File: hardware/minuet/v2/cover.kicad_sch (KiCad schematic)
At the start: 12 parts, among them J401 B2B-XH-A, U401 DRV8876PWPR

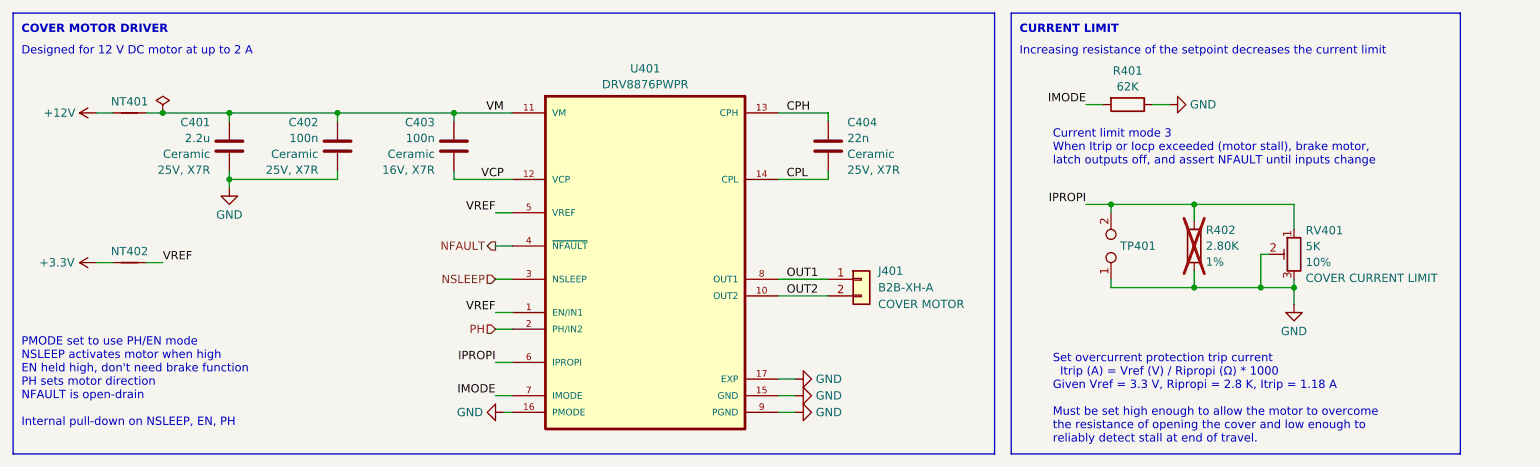
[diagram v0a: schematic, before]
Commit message: Finalize Minuet v2.1 for manufacture.
This revision uses a different motor controller and buck converter
and remedies errata from v2.0.
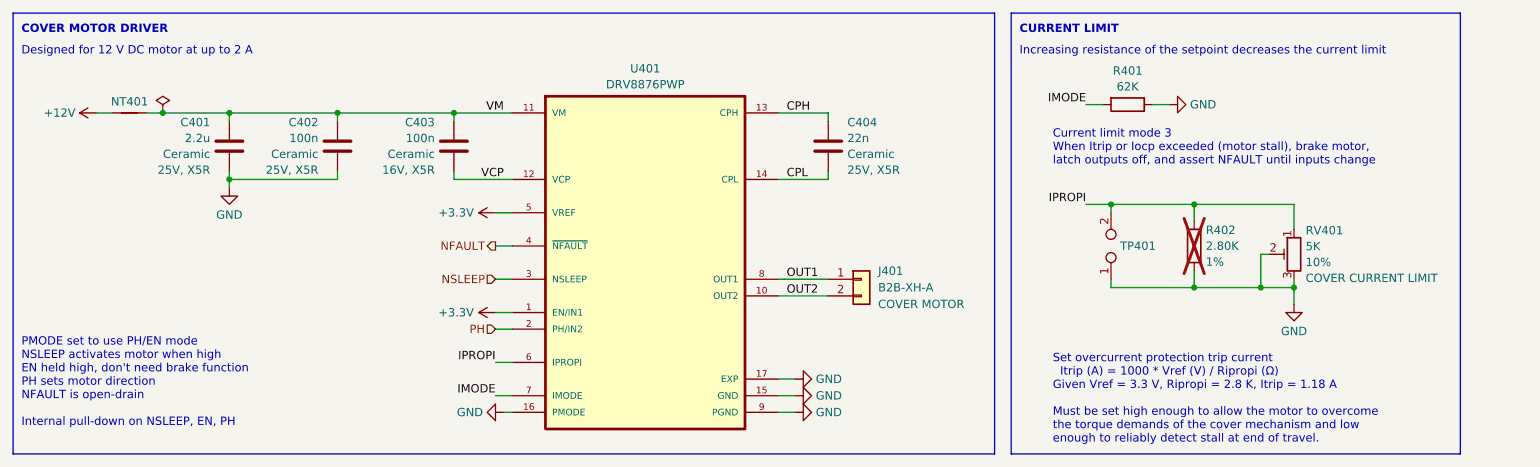
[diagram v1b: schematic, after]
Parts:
- removed NT402: NetTie_2, Generic:NetTie-2_SMD_Pad0.2mm, symbol Device:NetTie_2
- C401, C402, C404: Rating 25V, X7R -> 25V, X5R
- C403: Rating 16V, X7R -> 16V, X5R
- J401: LCSC (none) -> C158012
- RV401: LCSC (none) -> C81260
- U401: value DRV8876PWPR -> DRV8876PWP; LCSC (none) -> C575551
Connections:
- net VREF is gone; now on net +3.3V: U401.1 (EN/IN1), U401.5 (VREF)
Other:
- note added: "Set overcurrent protection trip current Itrip (A) = 1000 * Vref (V) / Ripropi (Ω) Given Vref = 3.3 V, Ripropi = 2.8 K, Itrip = 1.18 A Must be set high enough to allow the motor to overcome the torque demands of the cover mechanism and low enough to reliably detect stall at end of travel."
- note removed: "Set overcurrent protection trip current Itrip (A) = Vref (V) / Ripropi (Ω) * 1000 Given Vref = 3.3 V, Ripropi = 2.8 K, Itrip = 1.18 A Must be set high enough to allow the motor to overcome the resistance of opening the cover and low enough to reliably detect stall at end of travel."
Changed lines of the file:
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@@
 	(wire
 		(pts
-			(xy 55.88 95.25) (xy 58.42 95.25)
-		)
-		(stroke
-			(width 0)
-			(type default)
-		)
-	)
-	(wire
-		(pts
 			(xy 152.4 72.39) (xy 160.02 72.39)
 		)
@@
 	(wire
 		(pts
-			(xy 48.26 95.25) (xy 50.8 95.25)
-		)
-		(stroke
-			(width 0)
-			(type default)
-		)
-	)
-	(wire
-		(pts
 			(xy 209.55 71.12) (xy 212.09 71.12)
 		)
@@
 		)
 	)
-	(text "Set overcurrent protection trip current\n  Itrip (A) = Vref (V) / Ripropi (Ω) * 1000\nGiven Vref = 3.3 V, Ripropi = 2.8 K, Itrip = 1.18 A\n\nMust be set high enough to allow the motor to overcome\nthe resistance of opening the cover and low enough to\nreliably detect stall at end of travel."
+	(text "Set overcurrent protection trip current\n  Itrip (A) = 1000 * Vref (V) / Ripropi (Ω)\nGiven Vref = 3.3 V, Ripropi = 2.8 K, Itrip = 1.18 A\n\nMust be set high enough to allow the motor to overcome\nthe torque demands of the cover mechanism and low\nenough to reliably detect stall at end of travel."
 		(exclude_from_sim no)
 		(at 194.31 109.22 0)
@@
 		)
 	)
-	(label "VREF"
-		(at 109.22 102.87 180)
-		(effects
-			(font
-				(size 1.27 1.27)
-			)
-			(justify right bottom)
-		)
-	)
 	(label "VM"
 		(at 110.49 72.39 180)
@@
 		)
 	)
-	(label "VREF"
-		(at 58.42 95.25 0)
-		(effects
-			(font
-				(size 1.27 1.27)
-			)
-			(justify left bottom)
-		)
-	)
-	(label "VREF"
-		(at 109.22 87.63 180)
-		(effects
-			(font
-				(size 1.27 1.27)
-			)
-			(justify right bottom)
-		)
-	)
 	(label "CPH"
 		(at 153.67 72.39 0)
@@
 			)
 		)
-		(property "Rating" "25V, X7R"
+		(property "Rating" "25V, X5R"
 			(at 82.169 81.1064 0)
 			(effects
@@
 		(dnp no)
 		(fields_autoplaced yes)
-		(property "Reference" "#PWR0407"
+		(property "Reference" "#PWR0408"
 			(at 161.29 115.57 0)
 			(effects
@@
 			(project "minuet"
 				(path "/5bd7983a-3caa-4bb2-9dc5-1af533f31e50/713a3115-7b9d-4f98-8679-6fd4cf9d6fa9"
-					(reference "#PWR0407")
+					(reference "#PWR0408")
 					(unit 1)
 				)
@@
 		(dnp no)
 		(fields_autoplaced yes)
-		(property "Reference" "#PWR0408"
+		(property "Reference" "#PWR0409"
 			(at 104.14 118.11 0)
 			(effects
@@
 			(project "minuet"
 				(path "/5bd7983a-3caa-4bb2-9dc5-1af533f31e50/713a3115-7b9d-4f98-8679-6fd4cf9d6fa9"
-					(reference "#PWR0408")
+					(reference "#PWR0409")
 					(unit 1)
 				)
@@
 			)
 		)
-		(property "Rating" "25V, X7R"
+		(property "Rating" "25V, X5R"
 			(at 162.941 81.1064 0)
 			(effects
@@
 			)
 		)
-		(property "Rating" "16V, X7R"
+		(property "Rating" "16V, X5R"
 			(at 99.949 81.1064 0)
 			(effects
@@
 	)
 	(symbol
+		(lib_id "power:+3.3V")
+		(at 109.22 102.87 90)
+		(unit 1)
+		(exclude_from_sim no)
+		(in_bom yes)
+		(on_board yes)
+		(dnp no)
+		(property "Reference" "#PWR0406"
+			(at 113.03 102.87 0)
+			(effects
+				(font
+					(size 1.27 1.27)
+				)
+				(hide yes)
+			)
+		)
+		(property "Value" "+3.3V"
+			(at 105.918 102.87 90)
+			(effects
+				(font
+					(size 1.27 1.27)
+				)
+				(justify left)
+			)
+		)
+		(property "Footprint" ""
+			(at 109.22 102.87 0)
+			(effects
+				(font
+					(size 1.27 1.27)
+				)
+				(hide yes)
+			)
+		)
+		(property "Datasheet" ""
+			(at 109.22 102.87 0)
+			(effects
+				(font
+					(size 1.27 1.27)
+				)
+				(hide yes)
+			)
+		)
+		(property "Description" "Power symbol creates a global label with name \"+3.3V\""
+			(at 109.22 102.87 0)
+			(effects
+				(font
+					(size 1.27 1.27)
+				)
+				(hide yes)
+			)
+		)
+		(pin "1"
+		)
+		(instances
+			(project "minuet"
+				(path "/5bd7983a-3caa-4bb2-9dc5-1af533f31e50/713a3115-7b9d-4f98-8679-6fd4cf9d6fa9"
+					(reference "#PWR0406")
+					(unit 1)
+				)
+			)
+		)
+	)
+	(symbol
 		(lib_id "Device:NetTie_2")
 		(at 53.34 72.39 0)
@@
 			)
 		)
-		(property "Rating" "25V, X7R"
+		(property "Rating" "25V, X5R"
 			(at 65.659 81.1064 0)
 			(effects
@@
 	)
 	(symbol
-		(lib_id "Device:NetTie_2")
-		(at 53.34 95.25 0)
-		(unit 1)
-		(exclude_from_sim no)
-		(in_bom no)
-		(on_board yes)
-		(dnp no)
-		(fields_autoplaced yes)
-		(property "Reference" "NT402"
-			(at 53.34 93.5299 0)
-			(effects
-				(font
-					(size 1.27 1.27)
-				)
-			)
-		)
-		(property "Value" "NetTie_2"
-			(at 53.34 93.5298 0)
-			(effects
-				(font
-					(size 1.27 1.27)
-				)
-				(hide yes)
-			)
-		)
-		(property "Footprint" "Generic:NetTie-2_SMD_Pad0.2mm"
-			(at 53.34 95.25 0)
-			(effects
-				(font
-					(size 1.27 1.27)
-				)
-				(hide yes)
-			)
-		)
-		(property "Datasheet" "~"
-			(at 53.34 95.25 0)
-			(effects
-				(font
-					(size 1.27 1.27)
-				)
-				(hide yes)
-			)
-		)
-		(property "Description" "Net tie, 2 pins"
-			(at 53.34 95.25 0)
-			(effects
-				(font
-					(size 1.27 1.27)
-				)
-				(hide yes)
-			)
-		)
-		(pin "1"
-		)
-		(pin "2"
-		)
-		(instances
-			(project ""
-				(path "/5bd7983a-3caa-4bb2-9dc5-1af533f31e50/713a3115-7b9d-4f98-8679-6fd4cf9d6fa9"
-					(reference "NT402")
-					(unit 1)
-				)
-			)
-		)
-	)
-	(symbol
 		(lib_id "power:GND")
 		(at 231.14 101.6 0)
@@
 		(dnp no)
 		(fields_autoplaced yes)
-		(property "Reference" "#PWR0409"
+		(property "Reference" "#PWR0410"
 			(at 161.29 118.11 0)
 			(effects
@@
 			(project "minuet"
 				(path "/5bd7983a-3caa-4bb2-9dc5-1af533f31e50/713a3115-7b9d-4f98-8679-6fd4cf9d6fa9"
-					(reference "#PWR0409")
+					(reference "#PWR0410")
 					(unit 1)
 				)
@@
 		(dnp no)
 		(fields_autoplaced yes)
-		(property "Reference" "#PWR0406"
+		(property "Reference" "#PWR0407"
 			(at 161.29 113.03 0)
 			(effects
@@
 			(project "minuet"
 				(path "/5bd7983a-3caa-4bb2-9dc5-1af533f31e50/713a3115-7b9d-4f98-8679-6fd4cf9d6fa9"
-					(reference "#PWR0406")
+					(reference "#PWR0407")
 					(unit 1)
 				)
@@
 	(symbol
 		(lib_id "power:+3.3V")
-		(at 48.26 95.25 90)
+		(at 109.22 87.63 90)
 		(unit 1)
 		(exclude_from_sim no)
@@
 		(dnp no)
 		(property "Reference" "#PWR0404"
-			(at 52.07 95.25 0)
+			(at 113.03 87.63 0)
 			(effects
 				(font
@@
 		)
 		(property "Value" "+3.3V"
-			(at 44.958 95.25 90)
+			(at 105.918 87.63 90)
 			(effects
 				(font
@@
 		)
 		(property "Footprint" ""
-			(at 48.26 95.25 0)
+			(at 109.22 87.63 0)
 			(effects
 				(font
@@
 		)
 		(property "Datasheet" ""
-			(at 48.26 95.25 0)
+			(at 109.22 87.63 0)
 			(effects
 				(font
@@
 		)
 		(property "Description" "Power symbol creates a global label with name \"+3.3V\""
-			(at 48.26 95.25 0)
+			(at 109.22 87.63 0)
 			(effects
 				(font
@@
 		(on_board yes)
 		(dnp no)
-		(fields_autoplaced yes)
 		(property "Reference" "U401"
 			(at 132.08 65.6275 0)
@@
 			)
 		)
-		(property "Value" "DRV8876PWPR"
+		(property "Value" "DRV8876PWP"
 			(at 132.08 68.0518 0)
 			(effects
@@
 			)
 		)
+		(property "LCSC" "C575551"
+			(at 132.08 95.25 0)
+			(effects
+				(font
+					(size 1.27 1.27)
+				)
+				(hide yes)
+			)
+		)
 		(pin "17"
 		)
@@
 			)
 		)
+		(property "LCSC" "C81260"
+			(at 231.14 93.98 0)
+			(effects
+				(font
+					(size 1.27 1.27)
+				)
+				(hide yes)
+			)
+		)
 		(pin "1"
 		)
@@
 			)
 		)
+		(property "LCSC" "C158012"
+			(at 165.1 97.79 0)
+			(effects
+				(font
+					(size 1.27 1.27)
+				)
+				(hide yes)
+			)
+		)
